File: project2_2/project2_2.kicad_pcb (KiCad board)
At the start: 2 copper layers, 100.7 x 64 mm, 26 parts, among them J1 Conn_02x02, J2 Conn_02x03, J3 Conn_02x02, J4 Conn_02x02, U1 AT27C020, U2 AT27C020, U3 74LS670, U4 74LS670, U5 74LS32, U6 74LS00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

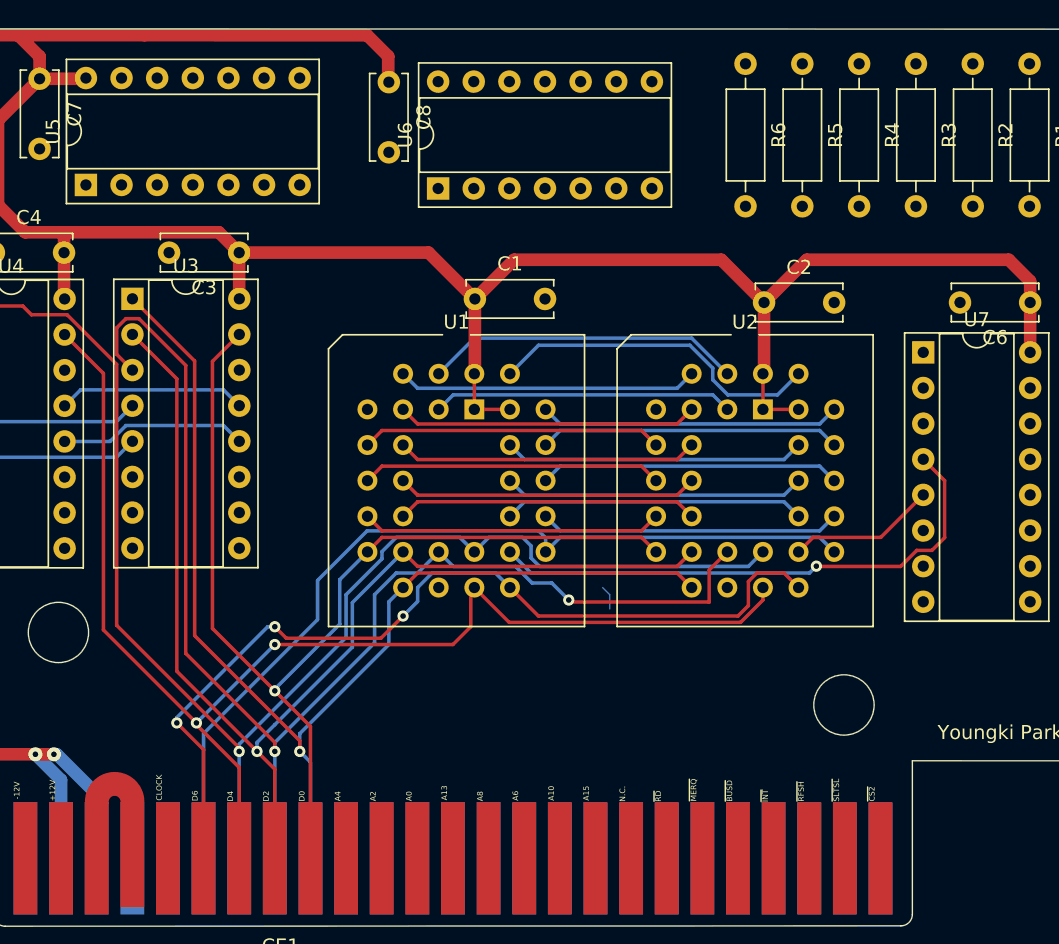
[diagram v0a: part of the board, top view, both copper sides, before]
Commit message: Modify PCB2-2
Signed-off-by: Youngki Park <ykp7409@gmail.com>
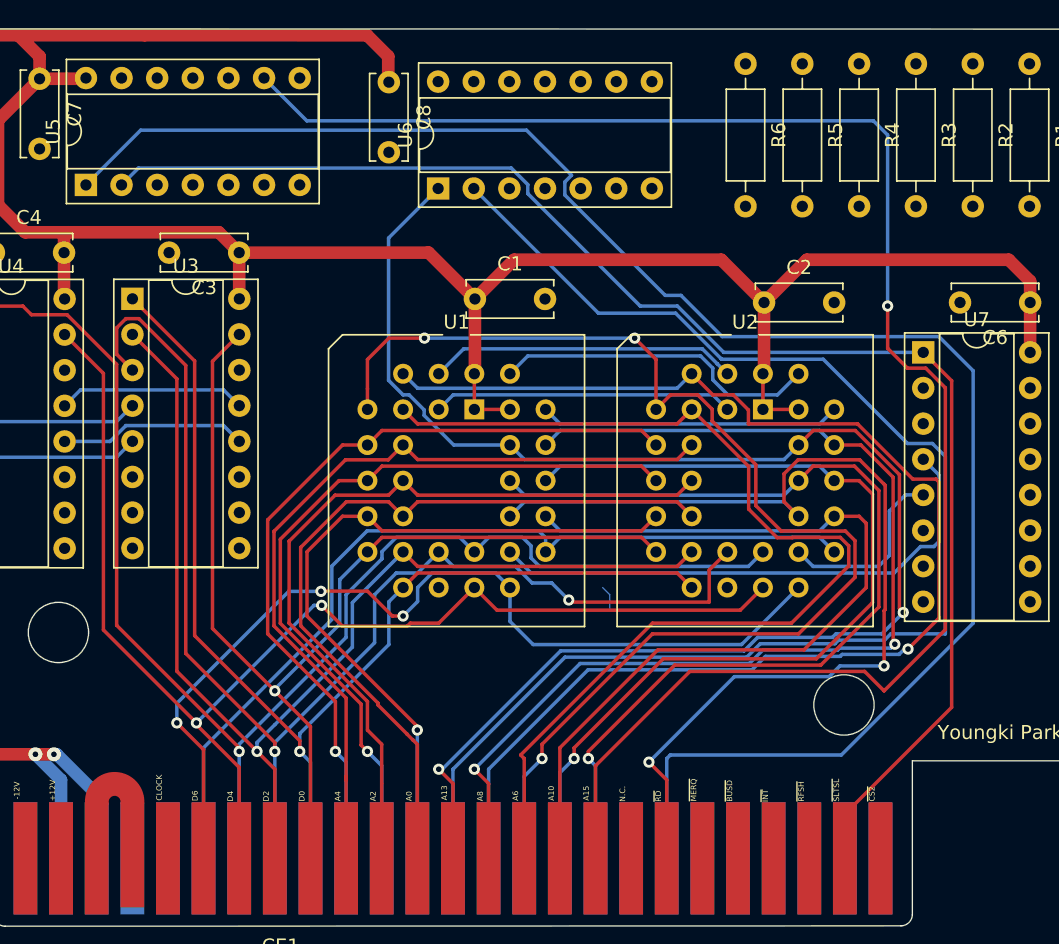
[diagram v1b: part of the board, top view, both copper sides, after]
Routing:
- net //WR: track 0.00 -> 124.4 mm
- net /A15: track 0.00 -> 120.6 mm, vias 0 -> 1
- net //SLTSL: track 0.00 -> 103.5 mm
- net /A14: track 0.00 -> 99.6 mm
- net /A13: track 21.4 -> 110.8 mm, vias 0 -> 2
- net /A7: track 0.00 -> 88.6 mm, vias 0 -> 3
- net /A12: track 21.4 -> 96.2 mm, vias 0 -> 1
- net /A8: track 21.4 -> 79.0 mm, vias 0 -> 2
- net /A6: track 21.4 -> 76.3 mm
- net //RD: track 21.4 -> 73.4 mm, vias 0 -> 2
- net /A9: track 21.4 -> 69.4 mm, vias 0 -> 1
- net /A11: track 21.4 -> 66.2 mm, vias 0 -> 1
- net /A10: track 21.4 -> 63.0 mm
- net /A4: track 21.4 -> 59.0 mm
- net /A5: track 21.4 -> 57.2 mm, vias 0 -> 1
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
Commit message: Modify pcb2-2
Signed-off-by: ykp74 <ykp7409@gmail.com>
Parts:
- moved R1 19.5 mm to (184.2, 90.7)
- moved R6 16.6 mm to (200.0, 90.7)
- moved R2 12.3 mm to (187.3, 90.7)
- moved R5 9.38 mm to (196.8, 90.7)
- moved R3 5.07 mm to (190.5, 90.7)
- moved R4 2.16 mm to (193.7, 90.7)
- moved U7 0.92 mm to (196.8, 111.8)
- moved C6 0.92 mm to (204.5, 108.2)
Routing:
- net Net-(U4-Q2): track 0.00 -> 149.5 mm, vias 0 -> 2
- net Net-(U4-Q1): track 0.00 -> 144.0 mm, vias 0 -> 2
- net /MA15: track 21.4 -> 115.5 mm, vias 0 -> 2
- net /MA17: track 23.4 -> 106.4 mm, vias 0 -> 2
- net /MA16: track 22.0 -> 104.6 mm, vias 0 -> 2
- net /A11: track 66.2 -> 146.6 mm
- net /MA14: track 21.4 -> 100.4 mm, vias 0 -> 2
- net /A15: track 120.6 -> 186.5 mm, vias 1 -> 2
- net /A12: track 96.2 -> 152.5 mm, vias 1 -> 3
- net GND: track 0.00 -> 49.5 mm, vias 0 -> 63
- net Net-(J1-Pin_2): track 0.00 -> 42.3 mm
- net Net-(J2-Pin_2): track 13.4 -> 37.6 mm
- net Net-(U5-Pad10): track 0.00 -> 23.3 mm
- net Net-(J4-Pin_2): track 13.4 -> 35.9 mm
- net Net-(U3-~{Ew}): track 13.4 -> 34.1 mm
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- added copper zone on B.Cu, net GND
- added copper zone on F.Cu, net GND
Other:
- board text added: "0"
- board text added: "A11"
- board text added: "A12"
- board text added: "A15"

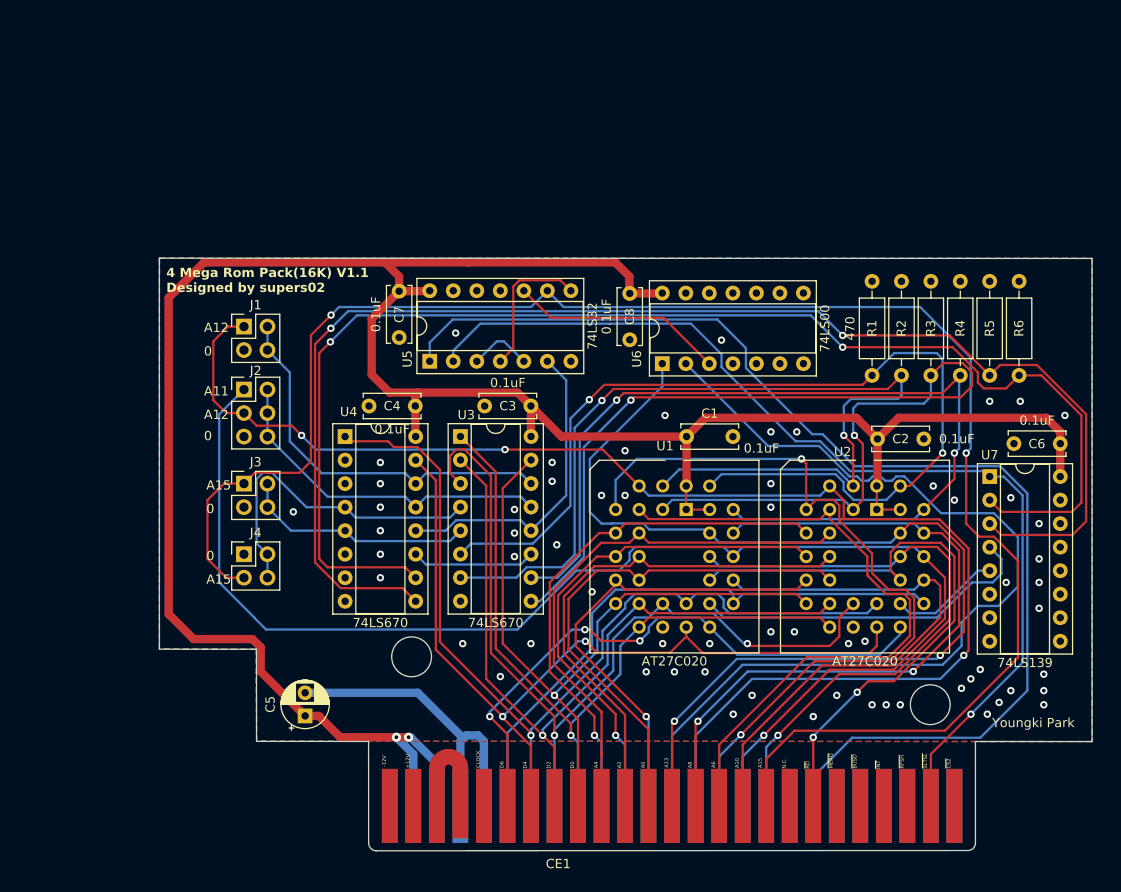
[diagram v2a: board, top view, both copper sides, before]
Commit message: Modify PCB2-2
Signed-off-by: Youngki Park <ykp7409@gmail.com>
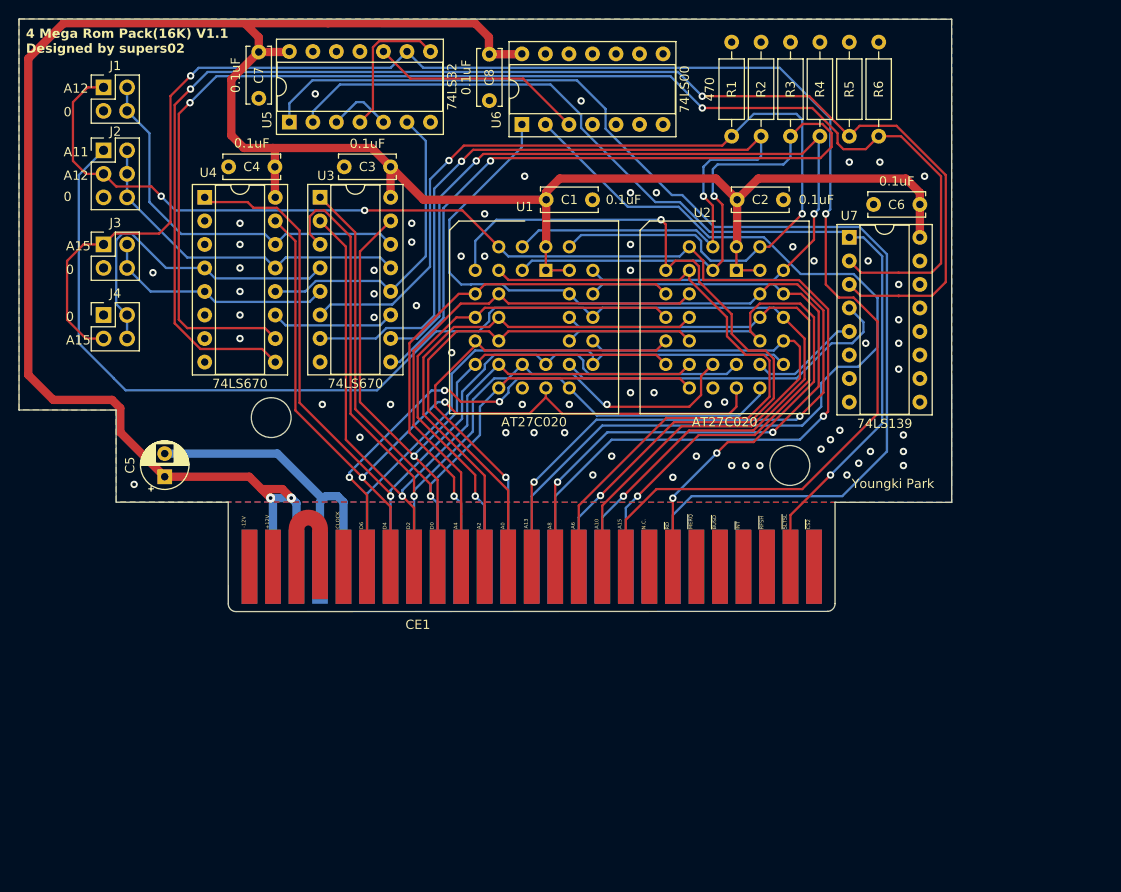
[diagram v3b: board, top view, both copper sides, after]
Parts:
- moved C5 29.9 mm to (107.8, 111.8)
- moved R4 29.9 mm to (178.5, 64.9)
- moved U6 29.9 mm to (146.3, 73.7)
- moved C4 29.9 mm to (114.7, 78.3)
- moved C7 29.9 mm to (117.9, 65.9)
- moved U3 29.9 mm to (124.6, 81.6)
- moved U4 29.9 mm to (112.1, 81.6)
- moved U5 29.9 mm to (121.2, 73.5)
- moved C2 29.9 mm to (169.6, 81.9)
- moved C3 29.9 mm to (132.2, 78.3)
- moved C6 29.9 mm to (189.3, 82.4)
- moved C8 29.9 mm to (142.8, 66.2)
- moved CE1 29.9 mm to (146.1, 118.3)
- moved J1 29.9 mm to (101.2, 69.7)
- moved J2 29.9 mm to (101.2, 76.5)
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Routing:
- net +5V: track 272.8 -> 278.1 mm
- net //WR: track 128.0 -> 129.5 mm
- net /A14: track 102.8 -> 102.1 mm
- net GND: vias 63 -> 64

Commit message: Modify PCB file
Signed-off-by: ykp74 <ykp7409@gmail.com>
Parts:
- moved C5 29.9 mm to (122.9, 137.6)
- moved R4 29.9 mm to (193.7, 90.7)
- moved U6 29.9 mm to (161.5, 99.6)
- moved C4 29.9 mm to (129.8, 104.1)
- moved C7 29.9 mm to (133.1, 91.7)
- moved U3 29.9 mm to (139.7, 107.4)
- moved U4 29.9 mm to (127.3, 107.4)
- moved U5 29.9 mm to (136.4, 99.3)
- moved C2 29.9 mm to (184.7, 107.7)
- moved C3 29.9 mm to (147.3, 104.1)
- moved C6 29.9 mm to (204.5, 108.2)
- moved C8 29.9 mm to (158.0, 92.0)
- moved CE1 29.9 mm to (161.3, 144.2)
- moved J1 29.9 mm to (116.3, 95.6)
- moved J2 29.9 mm to (116.3, 102.4)
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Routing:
- net +5V: track 278.1 -> 272.8 mm
- net //WR: track 129.5 -> 128.0 mm
- net /A14: track 102.1 -> 102.8 mm
- net GND: vias 64 -> 63

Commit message: Final revision
Signed-off-by: Youngki Park <ykp7409@gmail.com>
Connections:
- U4 pad 2: unconnected-(U4-D3-Pad2) -> GND
- U4 pad 3: unconnected-(U4-D4-Pad3) -> GND
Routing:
- net /D3: track 93.3 -> 94.5 mm
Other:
- board text added: "4 Mega Rom Pack(16K) V1.2 Designed by supers02"
- board text removed: "4 Mega Rom Pack(16K) V1.1 Designed by supers02"
